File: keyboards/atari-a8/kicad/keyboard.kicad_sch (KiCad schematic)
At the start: 210 parts, among them SW201 ESC, SW202 1, SW203 2, SW204 3, SW205 4, SW206 5, SW207 6, SW208 7, SW209 8, SW210 9, SW211 0, SW212 LT, SW213 GT, SW214 BS, SW215 C_UP, SW216 C_LEFT, SW217 C_DOWN, SW218 C_RIGHT, SW219 TAB, SW220 Q, SW221 W, SW222 E, SW223 R, SW224 T, SW225 Y, SW226 U, SW227 I, SW228 O, SW229 P, SW230 DASH, SW231 EQUAL, SW232 RET, SW233 HELP, SW234 RESET, SW235 OPTION, SW236 SELECT, SW237 CTRL, SW238 A, SW239 S, SW240 D, SW241 F, SW242 G, SW243 H, SW244 J, SW245 K, SW246 L, SW247 SEMI, SW248 PLUS, SW249 ASTRIX, SW250 CAPS, SW251 START, SW252 POWER, SW253 MENU, SW254 TURBO, SW255 FN, SW256 LSHIFT, SW257 Z, SW258 X, SW259 C, SW260 V, SW261 B, SW262 N, SW263 M, SW264 COMMA, SW265 PERIOD, SW266 SLASH, SW267 RSHIFT, SW268 INV, SW269 BREAK, SW270 SPACE

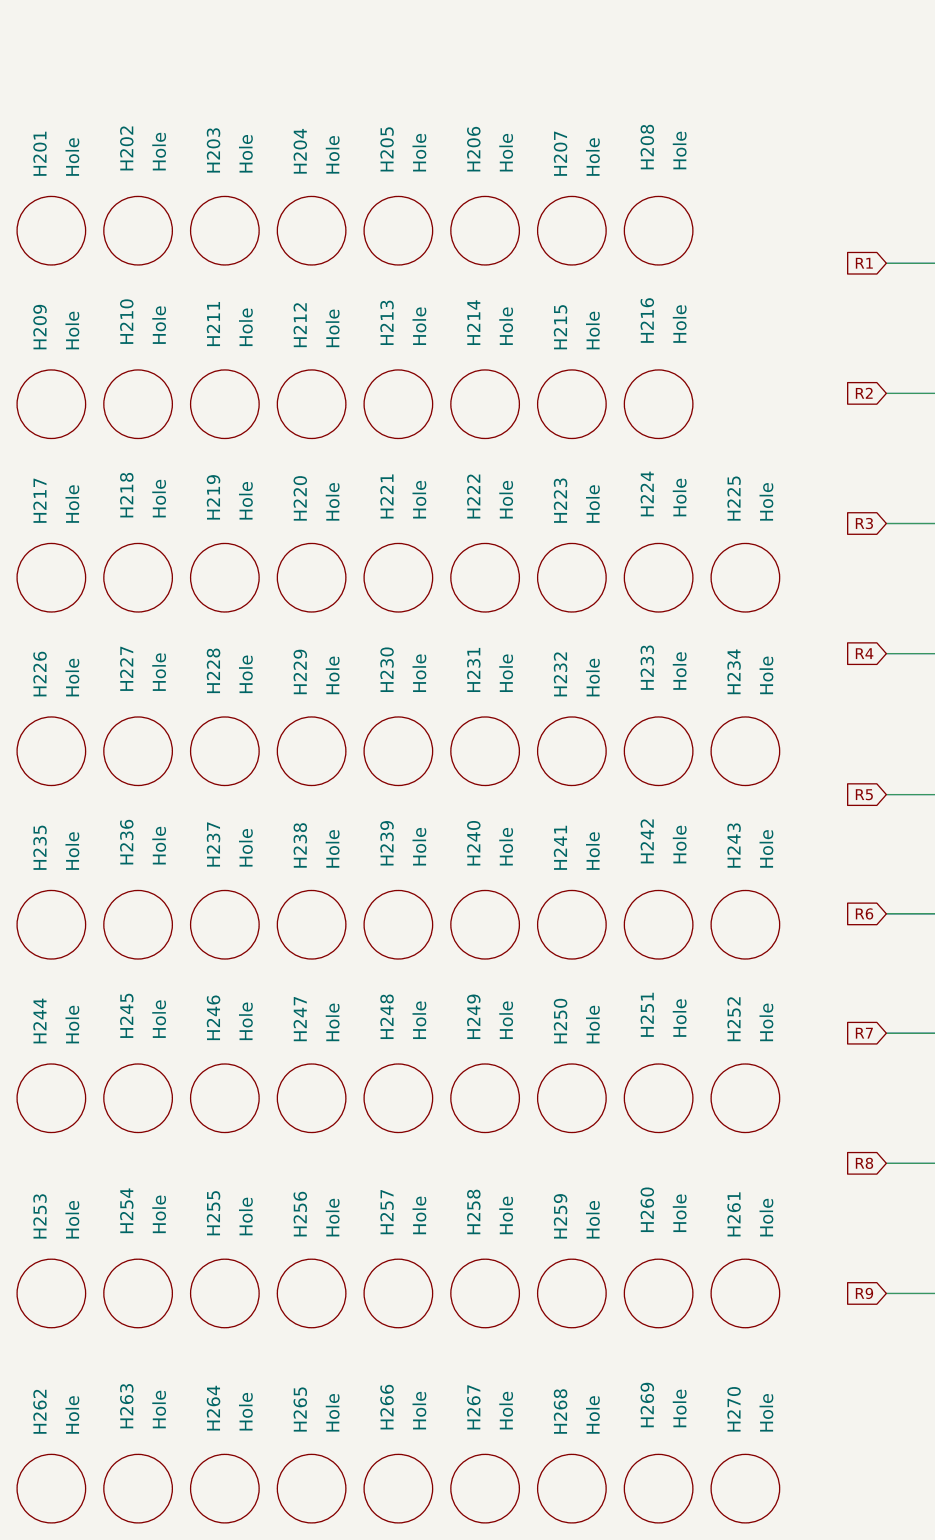
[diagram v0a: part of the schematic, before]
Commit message: Used new standoff holes and more track cleanup work.
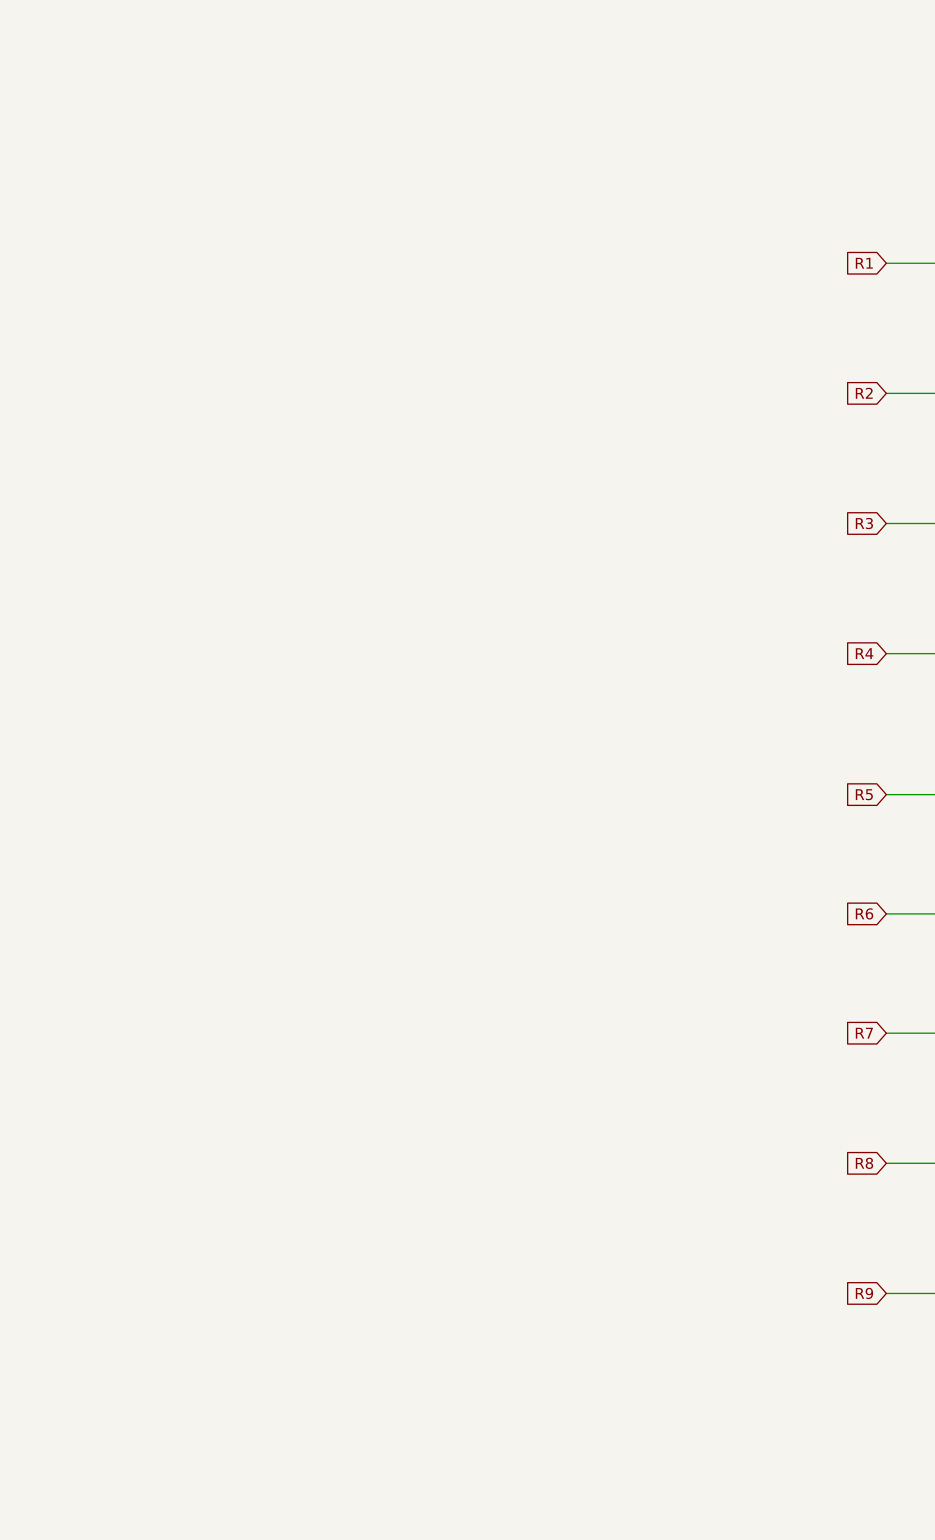
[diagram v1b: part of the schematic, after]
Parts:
- removed H201, H202, H203, H204, H205, H206, H207, H208, H209, H210, H211, H212, H213, H214, H215, H216, H217, H218, H219, H220, H221, H222, H223, H224, H225, H226, H227, H228, H229, H230, H231, H232, H233, H234, H235, H236, H237, H238, H239, H240, H241, H242, H243, H244, H245, H246, H247, H248, H249, H250, H251, H252, H253, H254, H255, H256, H257, H258, H259, H260, H261, H262, H263, H264, H265, H266, H267, H268, H269, H270: Hole, MountingHole:MountingHole_2.2mm_M2, symbol keebio:Hole
- SW232: PCB_X (none) -> 4; PCB_Y (none) -> 7
- SW256: PCB_Y (none) -> 5
